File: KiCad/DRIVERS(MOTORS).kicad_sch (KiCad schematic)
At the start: 17 parts, among them M1 Motor_DC, M2 Motor_DC, M3 Motor_DC, U11 ATtiny1616-M, U12 DRV8871DDA, U6 TB6612FNG

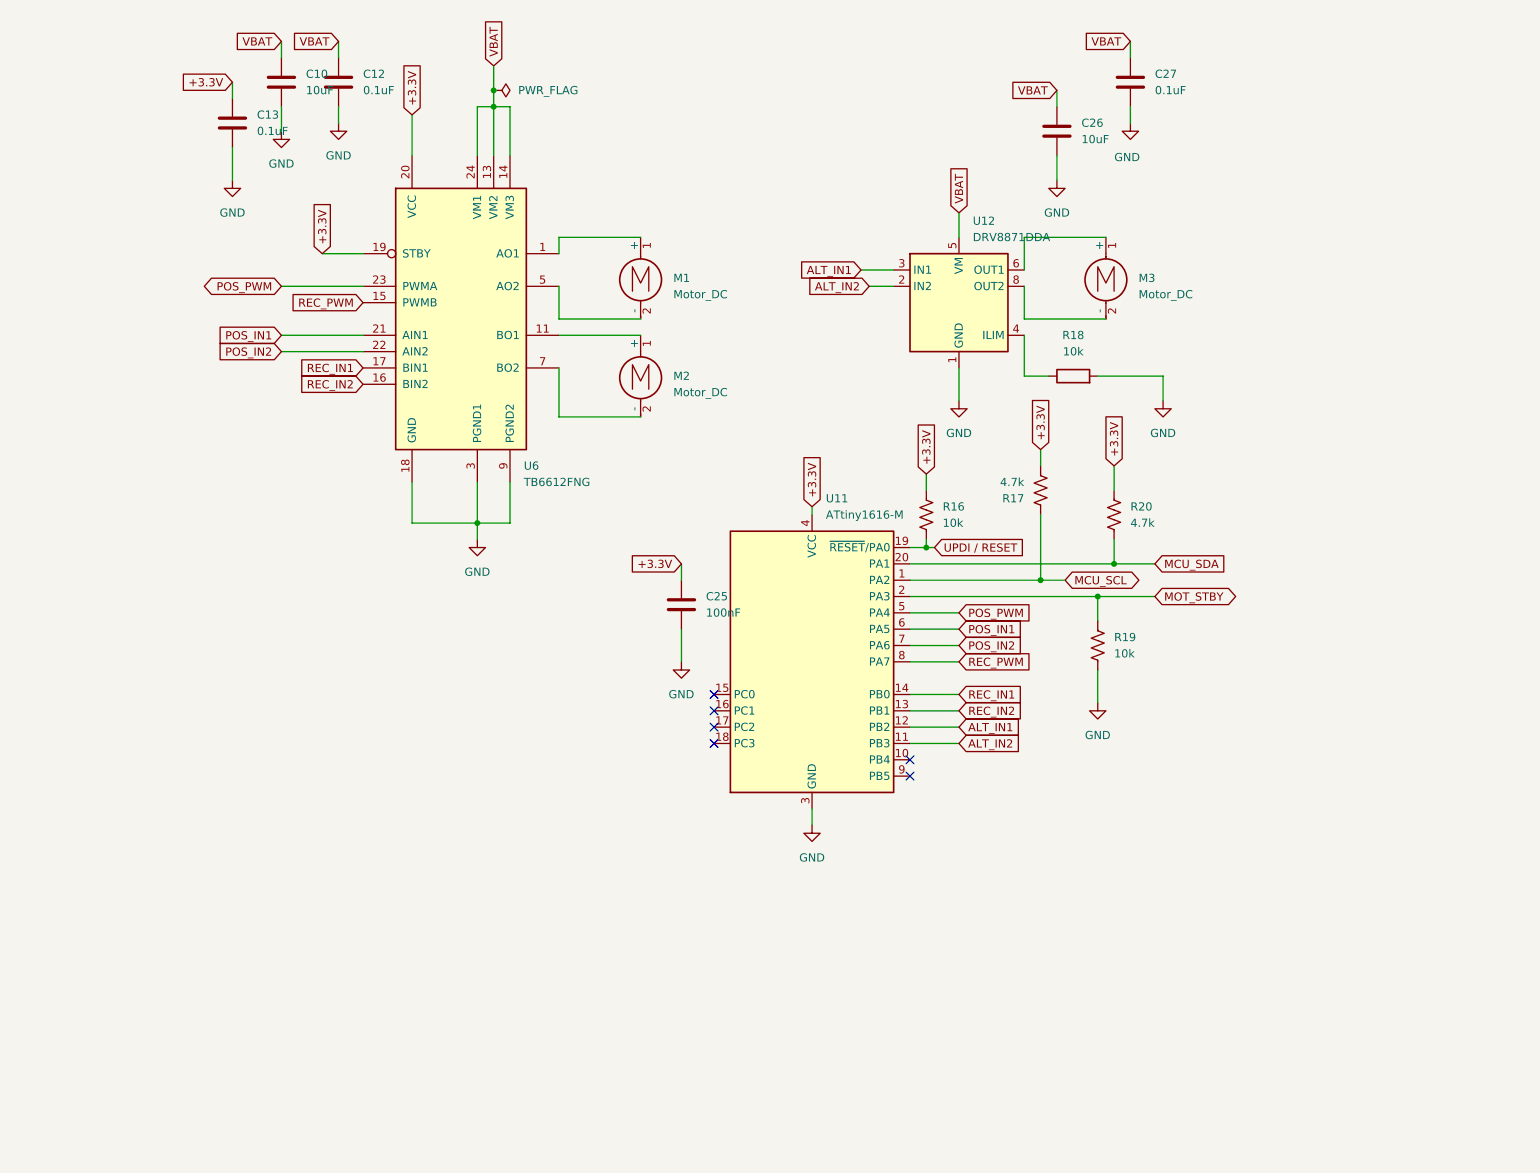
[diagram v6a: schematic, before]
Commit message: canvis a motors i layout
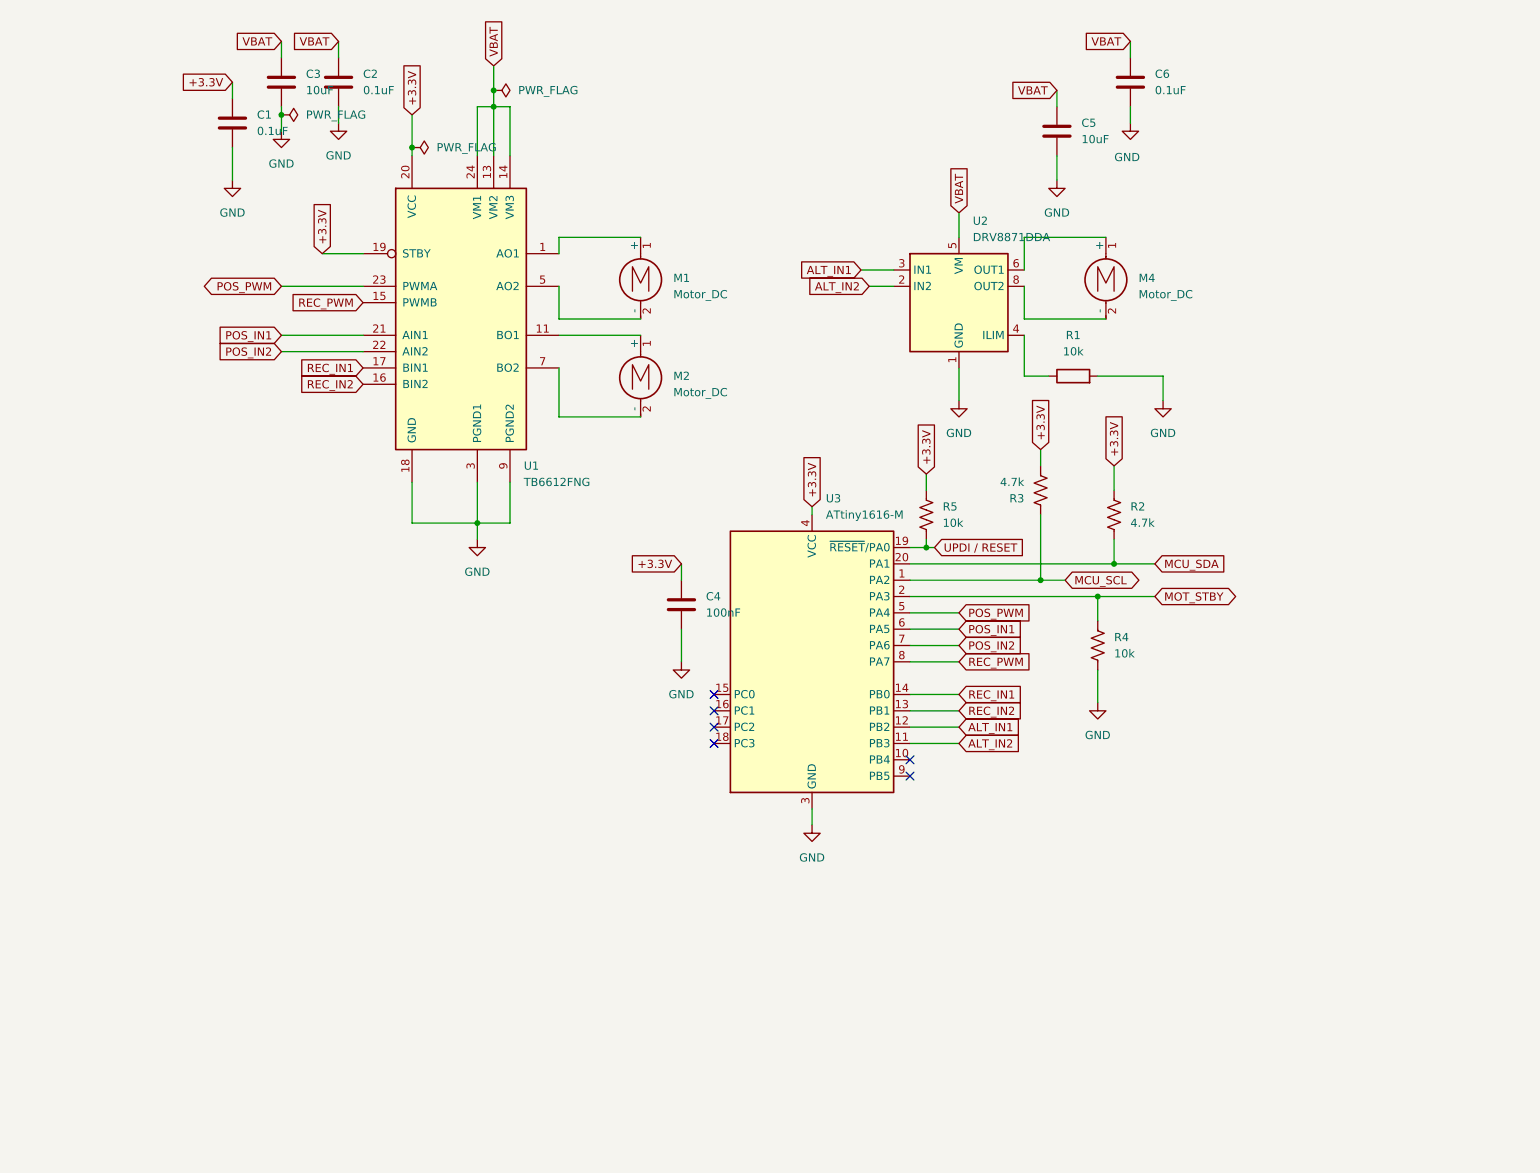
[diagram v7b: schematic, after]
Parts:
- C1: renamed from C13; footprint (none) -> Capacitor_SMD:C_0805_2012Metric
- C2: renamed from C12; footprint (none) -> Capacitor_SMD:C_0805_2012Metric
- C3: renamed from C10; footprint (none) -> Capacitor_THT:CP_Radial_D5.0mm_P2.50mm
- C4: renamed from C25; footprint (none) -> Capacitor_SMD:C_0805_2012Metric
- C5: renamed from C26; footprint (none) -> Capacitor_THT:CP_Radial_D5.0mm_P2.50mm
- C6: renamed from C27; footprint (none) -> Capacitor_SMD:C_0805_2012Metric
- M1, M2: footprint (none) -> Connector_PinHeader_2.54mm:PinHeader_1x02_P2.54mm_Horizontal
- M4: renamed from M3; footprint (none) -> Connector_PinHeader_2.54mm:PinHeader_1x02_P2.54mm_Horizontal
- renumbered R18 to R1, R20 to R2, R17 to R3, R19 to R4, R16 to R5, U6 to U1, U12 to U2, U11 to U3
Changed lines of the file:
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@@
 	)
 	(junction
+		(at 87.63 29.21)
+		(diameter 0)
+		(color 0 0 0 0)
+	)
+	(junction
 		(at 205.74 101.6)
 		(diameter 0)
@@
 	)
 	(junction
+		(at 107.95 34.29)
+		(diameter 0)
+		(color 0 0 0 0)
+	)
+	(junction
 		(at 118.11 92.71)
 		(diameter 0)
@@
 	(wire
 		(pts
-			(xy 107.95 29.21) (xy 107.95 35.56)
+			(xy 107.95 29.21) (xy 107.95 34.29)
 		)
 		(stroke
@@
 	(wire
 		(pts
+			(xy 107.95 34.29) (xy 107.95 35.56)
+		)
+		(stroke
+			(width 0)
+			(type default)
+		)
+	)
+	(wire
+		(pts
 			(xy 123.19 92.71) (xy 118.11 92.71)
 		)
@@
 	(wire
 		(pts
+			(xy 87.63 29.21) (xy 87.63 31.75)
+		)
+		(stroke
+			(width 0)
+			(type default)
+		)
+	)
+	(wire
+		(pts
 			(xy 205.74 101.6) (xy 209.55 101.6)
 		)
@@
 	(wire
 		(pts
-			(xy 87.63 27.94) (xy 87.63 31.75)
+			(xy 87.63 27.94) (xy 87.63 29.21)
 		)
 		(stroke
@@
 		(dnp no)
 		(fields_autoplaced yes)
-		(property "Reference" "R18"
+		(property "Reference" "R1"
 			(at 210.82 63.5 90)
 			(effects
@@
 		(dnp no)
 		(fields_autoplaced yes)
-		(property "Reference" "U12"
+		(property "Reference" "U2"
 			(at 195.1833 45.72 0)
 			(effects
@@
 			)
 		)
-		(property "Footprint" ""
+		(property "Footprint" "Connector_PinHeader_2.54mm:PinHeader_1x02_P2.54mm_Horizontal"
 			(at 143.51 55.626 0)
 			(effects
@@
 		(dnp no)
 		(fields_autoplaced yes)
-		(property "Reference" "R17"
+		(property "Reference" "R3"
 			(at 203.2 88.9001 0)
 			(effects
@@
 		(dnp no)
 		(fields_autoplaced yes)
-		(property "Reference" "C26"
+		(property "Reference" "C5"
 			(at 212.09 30.4799 0)
 			(effects
@@
 			)
 		)
-		(property "Footprint" ""
+		(property "Footprint" "Capacitor_THT:CP_Radial_D5.0mm_P2.50mm"
 			(at 209.2452 35.56 0)
 			(effects
@@
 		(dnp no)
 		(fields_autoplaced yes)
-		(property "Reference" "C10"
+		(property "Reference" "C3"
 			(at 91.44 22.8599 0)
 			(effects
@@
 			)
 		)
-		(property "Footprint" ""
+		(property "Footprint" "Capacitor_THT:CP_Radial_D5.0mm_P2.50mm"
 			(at 88.5952 27.94 0)
 			(effects
@@
 		(dnp no)
 		(fields_autoplaced yes)
-		(property "Reference" "C27"
+		(property "Reference" "C6"
 			(at 223.52 22.8599 0)
 			(effects
@@
 			)
 		)
-		(property "Footprint" ""
+		(property "Footprint" "Capacitor_SMD:C_0805_2012Metric"
 			(at 220.6752 27.94 0)
 			(effects
@@
 		(dnp no)
 		(fields_autoplaced yes)
-		(property "Reference" "#PWR018"
+		(property "Reference" "#PWR02"
 			(at 96.52 36.83 0)
 			(effects
@@
 		(dnp no)
 		(fields_autoplaced yes)
-		(property "Reference" "#PWR021"
+		(property "Reference" "#PWR04"
 			(at 118.11 101.6 0)
 			(effects
@@
 		(dnp no)
 		(fields_autoplaced yes)
-		(property "Reference" "C25"
+		(property "Reference" "C4"
 			(at 153.67 104.1399 0)
 			(effects
@@
 			)
 		)
-		(property "Footprint" ""
+		(property "Footprint" "Capacitor_SMD:C_0805_2012Metric"
 			(at 150.8252 109.22 0)
 			(effects
@@
 	)
 	(symbol
+		(lib_id "power:PWR_FLAG")
+		(at 107.95 34.29 270)
+		(unit 1)
+		(exclude_from_sim no)
+		(in_bom yes)
+		(on_board yes)
+		(dnp no)
+		(fields_autoplaced yes)
+		(property "Reference" "#FLG02"
+			(at 109.855 34.29 0)
+			(effects
+				(font
+					(size 1.27 1.27)
+				)
+				(hide yes)
+			)
+		)
+		(property "Value" "PWR_FLAG"
+			(at 111.76 34.2899 90)
+			(effects
+				(font
+					(size 1.27 1.27)
+				)
+				(justify left)
+			)
+		)
+		(property "Footprint" ""
+			(at 107.95 34.29 0)
+			(effects
+				(font
+					(size 1.27 1.27)
+				)
+				(hide yes)
+			)
+		)
+		(property "Datasheet" "~"
+			(at 107.95 34.29 0)
+			(effects
+				(font
+					(size 1.27 1.27)
+				)
+				(hide yes)
+			)
+		)
+		(property "Description" "Special symbol for telling ERC where power comes from"
+			(at 107.95 34.29 0)
+			(effects
+				(font
+					(size 1.27 1.27)
+				)
+				(hide yes)
+			)
+		)
+		(pin "1"
+		)
+		(instances
+			(project "DRIVERS(MOTORS)"
+				(path "/7b02ed73-5e8a-4db8-ad9f-4f6390d1b355"
+					(reference "#FLG02")
+					(unit 1)
+				)
+			)
+		)
+	)
+	(symbol
 		(lib_id "power:GND")
 		(at 80.01 39.37 0)
@@
 		(dnp no)
 		(fields_autoplaced yes)
-		(property "Reference" "#PWR019"
+		(property "Reference" "#PWR03"
 			(at 80.01 45.72 0)
 			(effects
@@
 		(dnp no)
 		(fields_autoplaced yes)
-		(property "Reference" "#FLG011"
+		(property "Reference" "#FLG03"
 			(at 122.555 25.4 0)
 			(effects
@@
 		(dnp no)
 		(fields_autoplaced yes)
-		(property "Reference" "#PWR041"
+		(property "Reference" "#PWR05"
 			(at 193.04 80.01 0)
 			(effects
@@
 		(on_board yes)
 		(dnp no)
-		(property "Reference" "#PWR044"
+		(property "Reference" "#PWR011"
 			(at 219.71 36.83 0)
 			(effects
@@
 		(dnp no)
 		(fields_autoplaced yes)
-		(property "Reference" "#PWR040"
+		(property "Reference" "#PWR07"
 			(at 170.18 146.05 0)
 			(effects
@@
 		(dnp no)
 		(fields_autoplaced yes)
-		(property "Reference" "M3"
+		(property "Reference" "M4"
 			(at 220.98 54.6099 0)
 			(effects
@@
 			)
 		)
-		(property "Footprint" ""
+		(property "Footprint" "Connector_PinHeader_2.54mm:PinHeader_1x02_P2.54mm_Horizontal"
 			(at 215.9 55.626 0)
 			(effects
@@
 		(dnp no)
 		(fields_autoplaced yes)
-		(property "Reference" "R20"
+		(property "Reference" "R2"
 			(at 219.71 90.1699 0)
 			(effects
@@
 		(dnp no)
 		(fields_autoplaced yes)
-		(property "Reference" "U6"
+		(property "Reference" "U1"
 			(at 125.3333 83.82 0)
 			(effects
@@
 		(dnp no)
 		(fields_autoplaced yes)
-		(property "Reference" "U11"
+		(property "Reference" "U3"
 			(at 172.3233 88.9 0)
 			(effects
@@
 		(dnp no)
 		(fields_autoplaced yes)
-		(property "Reference" "#PWR045"
+		(property "Reference" "#PWR06"
 			(at 224.79 80.01 0)
 			(effects
@@
 		(dnp no)
 		(fields_autoplaced yes)
-		(property "Reference" "#PWR016"
+		(property "Reference" "#PWR01"
 			(at 87.63 38.1 0)
 			(effects
@@
 	)
 	(symbol
+		(lib_id "power:PWR_FLAG")
+		(at 87.63 29.21 270)
+		(unit 1)
+		(exclude_from_sim no)
+		(in_bom yes)
+		(on_board yes)
+		(dnp no)
+		(fields_autoplaced yes)
+		(property "Reference" "#FLG01"
+			(at 89.535 29.21 0)
+			(effects
+				(font
+					(size 1.27 1.27)
+				)
+				(hide yes)
+			)
+		)
+		(property "Value" "PWR_FLAG"
+			(at 91.44 29.2099 90)
+			(effects
+				(font
+					(size 1.27 1.27)
+				)
+				(justify left)
+			)
+		)
+		(property "Footprint" ""
+			(at 87.63 29.21 0)
+			(effects
+				(font
+					(size 1.27 1.27)
+				)
+				(hide yes)
+			)
+		)
+		(property "Datasheet" "~"
+			(at 87.63 29.21 0)
+			(effects
+				(font
+					(size 1.27 1.27)
+				)
+				(hide yes)
+			)
+		)
+		(property "Description" "Special symbol for telling ERC where power comes from"
+			(at 87.63 29.21 0)
+			(effects
+				(font
+					(size 1.27 1.27)
+				)
+				(hide yes)
+			)
+		)
+		(pin "1"
+		)
+		(instances
+			(project "DRIVERS(MOTORS)"
+				(path "/7b02ed73-5e8a-4db8-ad9f-4f6390d1b355"
+					(reference "#FLG01")
+					(unit 1)
+				)
+			)
+		)
+	)
+	(symbol
 		(lib_id "power:GND")
 		(at 208.28 39.37 0)
@@
 		(dnp no)
 		(fields_autoplaced yes)
-		(property "Reference" "#PWR042"
+		(property "Reference" "#PWR010"
 			(at 208.28 45.72 0)
 			(effects
@@
 		(dnp no)
 		(fields_autoplaced yes)
-		(property "Reference" "R16"
+		(property "Reference" "R5"
 			(at 190.5 90.1699 0)
 			(effects
@@
 		(dnp no)
 		(fields_autoplaced yes)
-		(property "Reference" "C12"
+		(property "Reference" "C2"
 			(at 100.33 22.8599 0)
 			(effects
@@
 			)
 		)
-		(property "Footprint" ""
+		(property "Footprint" "Capacitor_SMD:C_0805_2012Metric"
 			(at 97.4852 27.94 0)
 			(effects
@@
 		(dnp no)
 		(fields_autoplaced yes)
-		(property "Reference" "#PWR039"
+		(property "Reference" "#PWR08"
 			(at 149.86 120.65 0)
 			(effects
@@
 		(dnp no)
 		(fields_autoplaced yes)
-		(property "Reference" "#PWR043"
+		(property "Reference" "#PWR09"
 			(at 214.63 127 0)
 			(effects
@@
 			)
 		)
-		(property "Footprint" ""
+		(property "Footprint" "Connector_PinHeader_2.54mm:PinHeader_1x02_P2.54mm_Horizontal"
 			(at 143.51 70.866 0)
 			(effects
@@
 		(dnp no)
 		(fields_autoplaced yes)
-		(property "Reference" "C13"
+		(property "Reference" "C1"
 			(at 83.82 29.2099 0)
 			(effects
@@
 			)
 		)
-		(property "Footprint" ""
+		(property "Footprint" "Capacitor_SMD:C_0805_2012Metric"
 			(at 80.9752 34.29 0)
 			(effects
@@
 		(dnp no)
 		(fields_autoplaced yes)
-		(property "Reference" "R19"
+		(property "Reference" "R4"
 			(at 217.17 110.4899 0)
 			(effects
